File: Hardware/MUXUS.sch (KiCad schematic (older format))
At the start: 124 parts, among them J1 USB_C_Receptacle_USB2.0, J10 VCP, J2 USB_B, J3 USB_A, J4 USB_B, J5 USB_A, J6 STDC14, J7 USB_B, J8 USB_A, J9 SWD, SW1 USER, SW2 RESET, U1 USBLC6-4SC6, U10 AP2151W, U11 AOZ1212AI, U12 USBLC6-2SC6, U13 USBLC6-2SC6, U14 AP2151W, U2 USB2504A-JT, U3 USBLC6-2SC6, U4 USBLC6-2SC6, U5 AP2151W, U6 TS3USBCA420RSVR, U8 USBLC6-2SC6, U9 USBLC6-2SC6, Y1 ATS240C

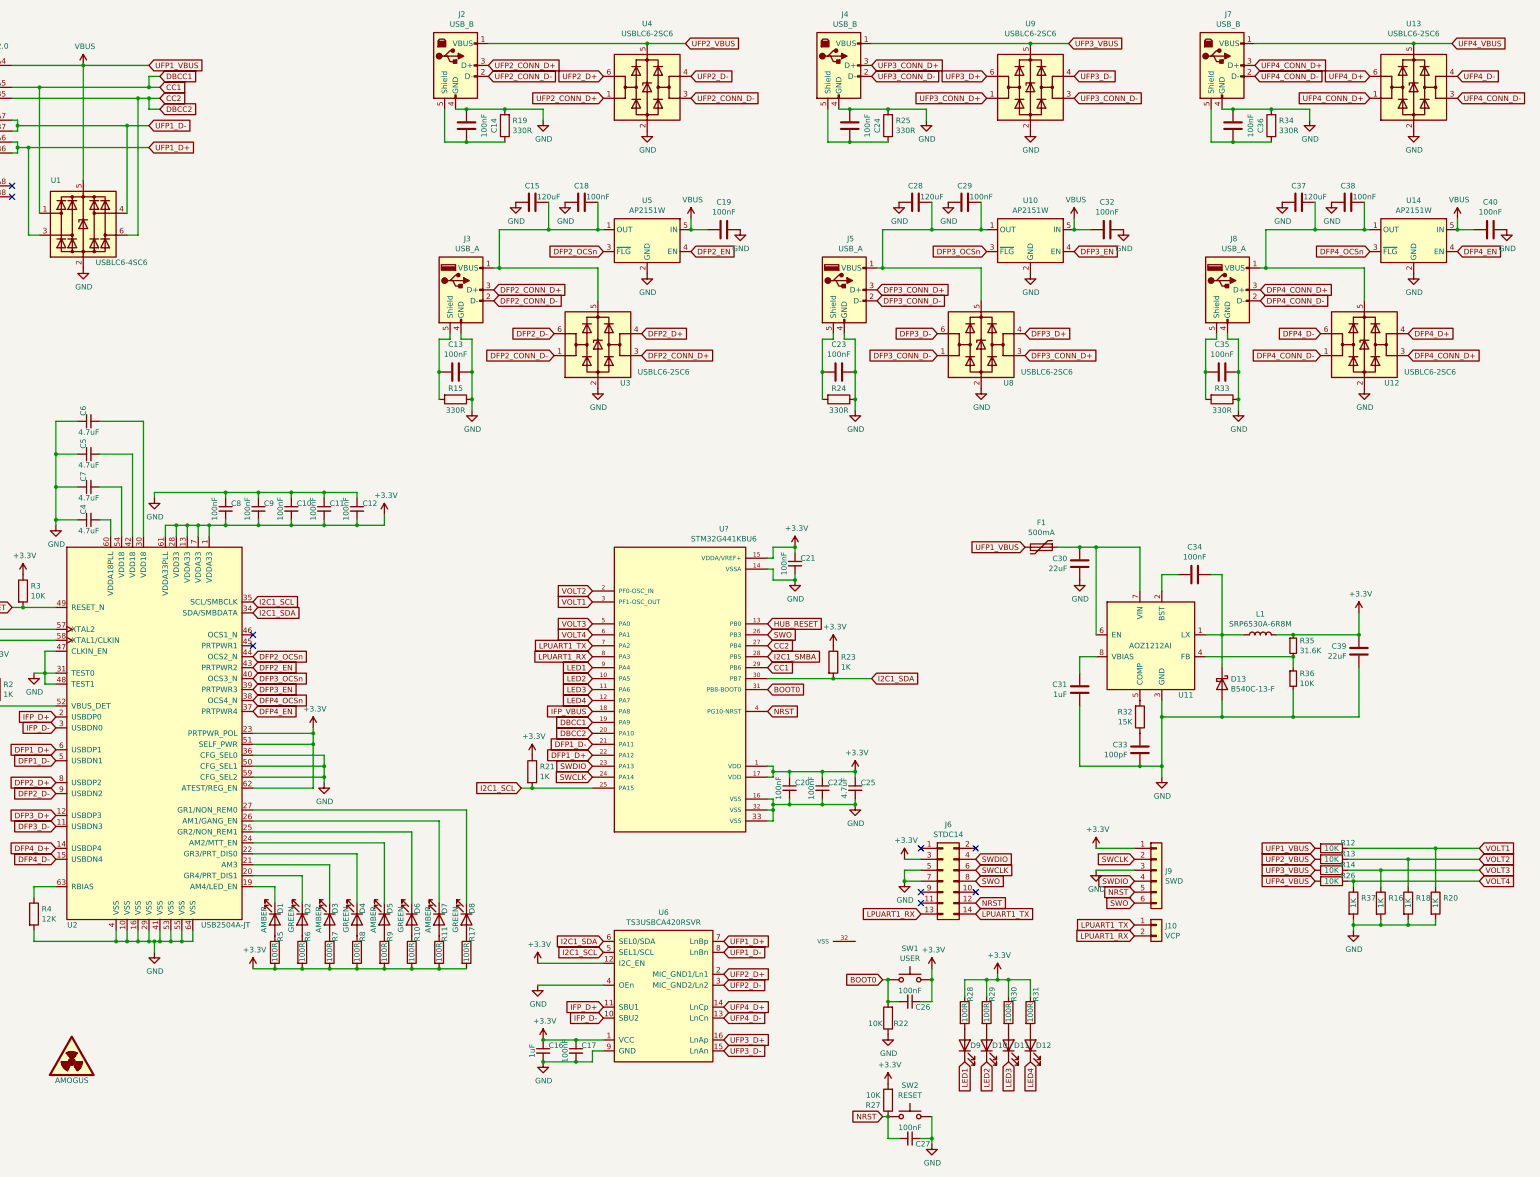
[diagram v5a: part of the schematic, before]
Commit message: Repaired routing and fixed some 3d models
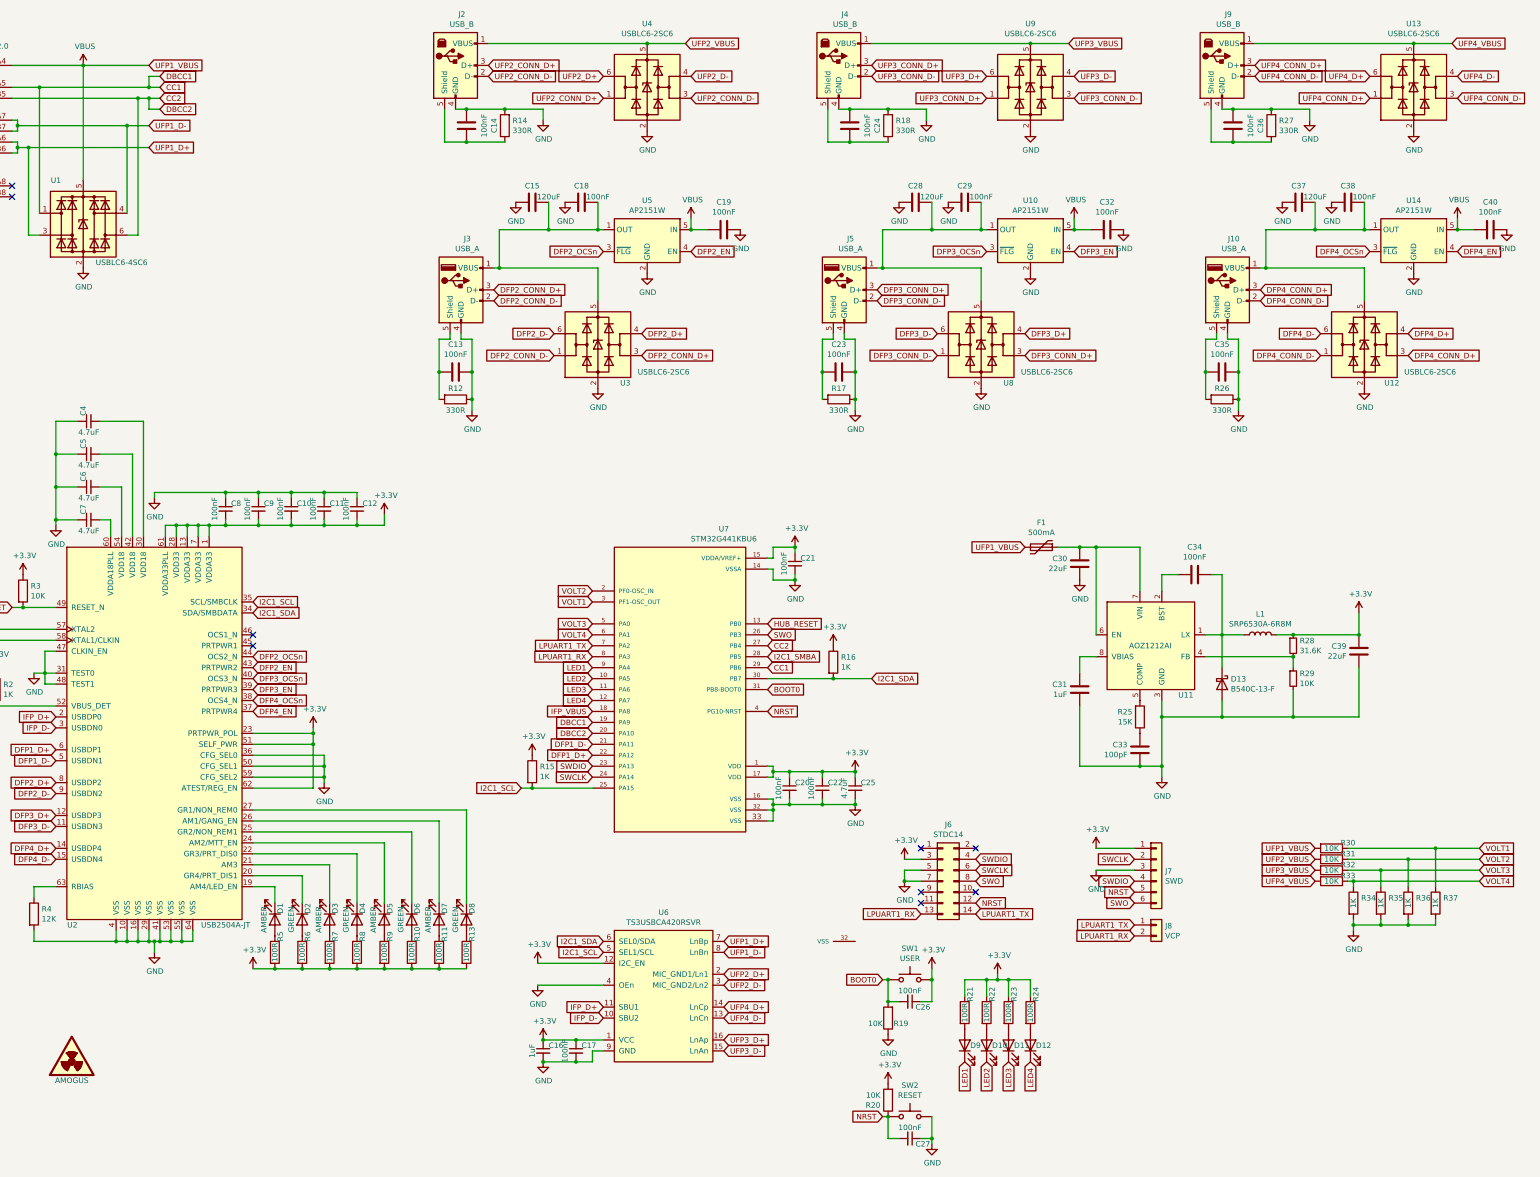
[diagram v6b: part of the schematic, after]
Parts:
- gave numbers to parts that had none: 1
- renumbered C6 to C4, C7 to C6, C4 to C7, J8 to J10, J9 to J7, J10 to J8, J7 to J9, R15 to R12, R17 to R13, R19 to R14, R21 to R15, R23 to R16, R24 to R17, R25 to R18, R22 to R19, R27 to R20, R28 to R21, R29 to R22, R30 to R23, R31 to R24, R32 to R25, R33 to R26, R34 to R27, R35 to R28, R36 to R29, R12 to R30, R13 to R31, R14 to R32, R26 to R33, R37 to R34, R16 to R35, R18 to R36, R20 to R37

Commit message: USB, mux and 3d models update
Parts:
- J1: footprint DX07S016JA1R1500:DX07S016JA1R1500 -> USB4110-GF-A:USB4110-GF-A
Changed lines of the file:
@@
 F 0 "J1" H 1507 2567 50  0000 C CNN
 F 1 "USB_C_Receptacle_USB2.0" H 1507 2476 50  0000 C CNN
-F 2 "DX07S016JA1R1500:DX07S016JA1R1500" H 1550 1700 50  0001 C CNN
+F 2 "USB4110-GF-A:USB4110-GF-A" H 1550 1700 50  0001 C CNN
 F 3 "https://www.usb.org/sites/default/files/documents/usb_type-c.zip" H 1550 1700 50  0001 C CNN
 	1    1400 1700

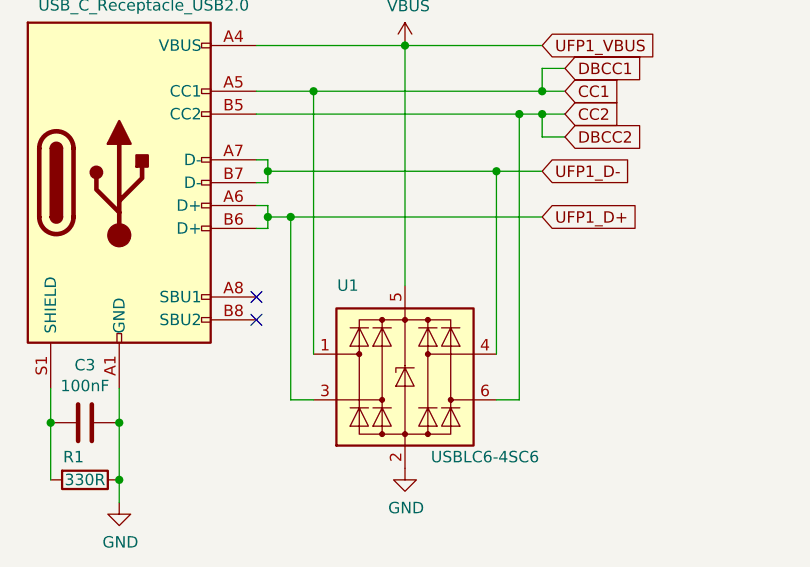
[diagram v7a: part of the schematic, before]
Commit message: Update UFP1 routing
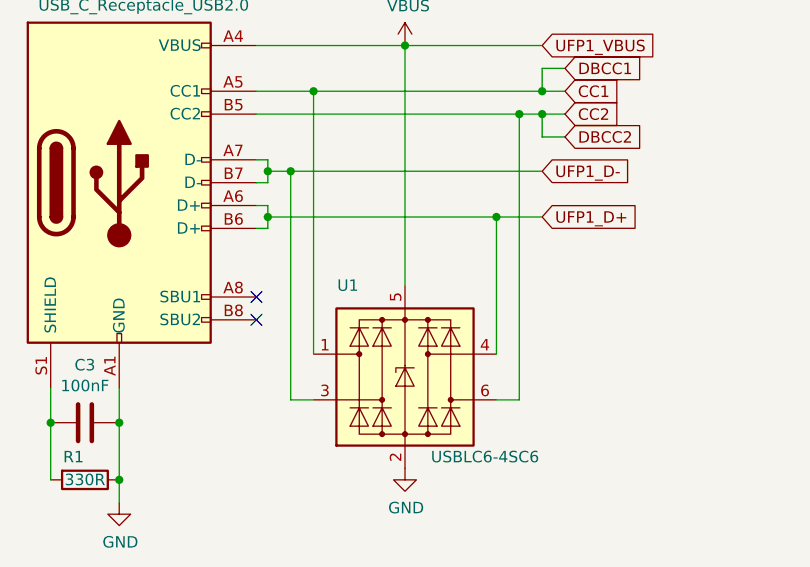
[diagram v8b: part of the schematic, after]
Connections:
- net UFP1_D+: now also U1.4 (I/O3); no longer U1.3 (I/O2)
- net UFP1_D-: now also U1.3 (I/O2); no longer U1.4 (I/O3)
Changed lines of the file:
@@
 	1    0    0    -1
 $EndComp
-$Comp
-L Power_Protection:USBLC6-4SC6 U1
-U 1 1 61A4E349
-P 2650 2550
-F 0 "U1" H 2400 2950 50  0000 C CNN
-F 1 "USBLC6-4SC6" H 3000 2200 50  0000 C CNN
-F 2 "Package_TO_SOT_SMD:SOT-23-6" H 2650 2050 50  0001 C CNN
-F 3 "https://www.st.com/resource/en/datasheet/usblc6-4.pdf" H 2850 2900 50  0001 C CNN
-	1    2650 2550
-	1    0    0    -1
-$EndComp
-Wire Wire Line
-	2050 1850 2150 1850
-Wire Wire Line
-	2150 2650 2150 1850
-Connection ~ 2150 1850
-Wire Wire Line
-	2150 1850 3250 1850
-Wire Wire Line
-	3050 2450 3050 1650
-Wire Wire Line
-	2050 1650 3050 1650
-Connection ~ 3050 1650
-Wire Wire Line
-	3050 1650 3250 1650
+Wire Wire Line
+	2050 1650 2150 1650
 Wire Wire Line
 	3000 4950 3000 5400
@@
 	8950 8000 8950 7900
 Connection ~ 8950 7900
+Wire Wire Line
+	2050 1850 3050 1850
+Wire Wire Line
+	2150 2650 2150 1650
+Connection ~ 2150 1650
+Wire Wire Line
+	2150 1650 3250 1650
+$Comp
+L Power_Protection:USBLC6-4SC6 U1
+U 1 1 61A4E349
+P 2650 2550
+F 0 "U1" H 2400 2950 50  0000 C CNN
+F 1 "USBLC6-4SC6" H 3000 2200 50  0000 C CNN
+F 2 "Package_TO_SOT_SMD:SOT-23-6" H 2650 2050 50  0001 C CNN
+F 3 "https://www.st.com/resource/en/datasheet/usblc6-4.pdf" H 2850 2900 50  0001 C CNN
+	1    2650 2550
+	1    0    0    -1
+$EndComp
+Wire Wire Line
+	3050 2450 3050 1850
+Connection ~ 3050 1850
+Wire Wire Line
+	3050 1850 3250 1850
 $EndSCHEMATC
